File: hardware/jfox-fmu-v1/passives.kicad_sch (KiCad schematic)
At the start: 43 parts, among them X1 16MHz, X2 32.768kHz

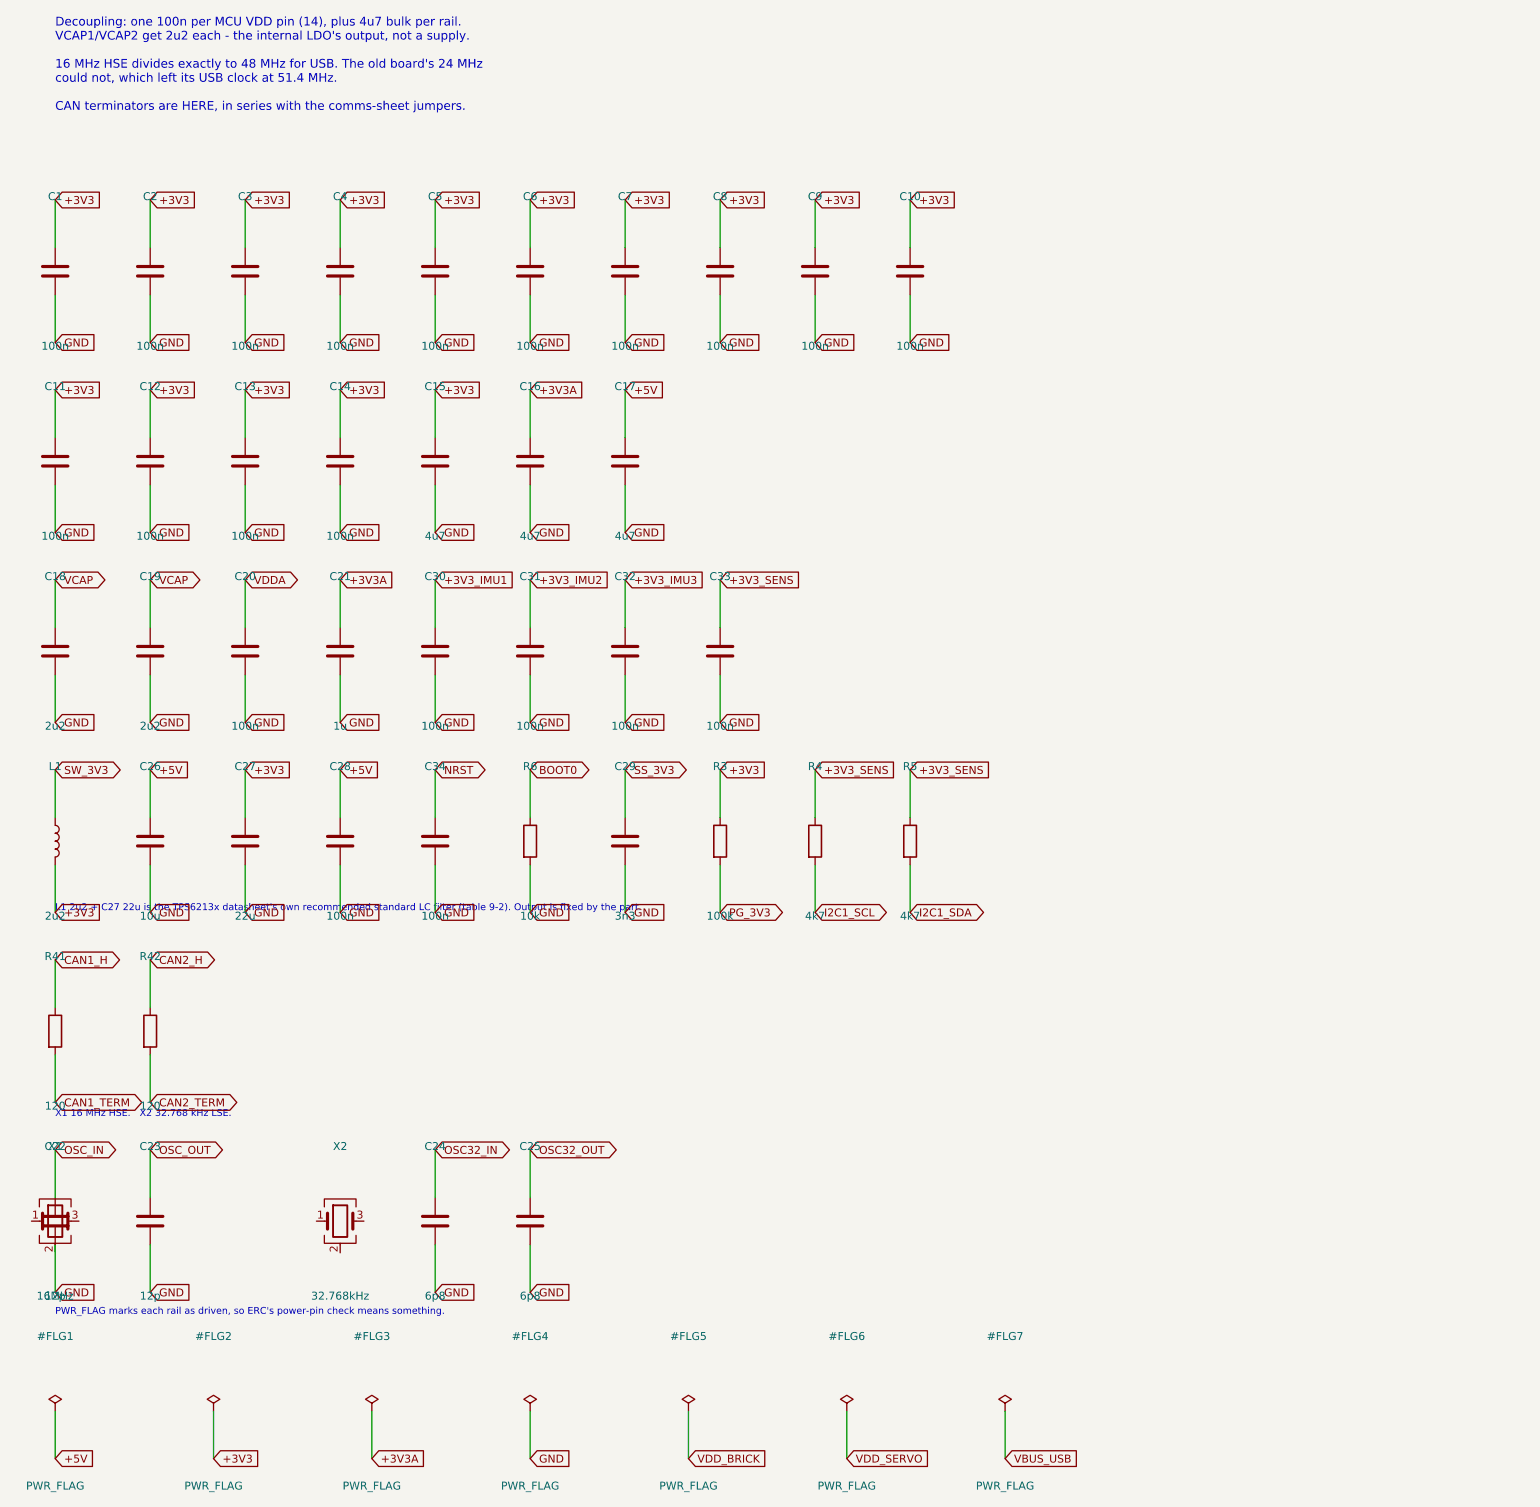
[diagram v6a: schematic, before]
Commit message: Isolated CAN FD, and the short it took a bisect to find
CAN redundancy is resolved by using Cyphal. FDCAN1 and FDCAN2 become two
redundant Cyphal/CAN interfaces on two independent isolated buses.

That is not the compromise it looked like. Cyphal handles redundancy in the
protocol: the specification defines redundant transport groups where a node
publishes on every interface and the receiver deduplicates, per frame or per
transfer. libcanard gives each redundant interface its own TX queue for
exactly this. So two controllers is the arrangement Cyphal is built around,
and it buys controller-level redundancy rather than the isolator-level
redundancy that keeping two separate buses would have given. The "four
controllers needed, two available" constraint dissolves rather than binds.

Better still, if wanted later: Cyphal supports heterogeneous redundancy, so a
Cyphal/CAN interface paired with Cyphal/UDP would give dissimilar transport
redundancy - the same argument that puts three IMUs from two vendors here.

U30/U31 become ISOW1044: isolated CAN FD with an integrated isolated DC-DC, so
each bus gets its own supply domain without a separate converter. Two
datasheet shorts that are easy to miss and both mandatory (SLLSFF7A table
7-1): GNDIO and GND1 are not internally connected, and VISOOUT/VSIN/VISOIN are
one node. EN/FLT is wired as the fault output with a 10k pull-up, because a
redundant link whose failure is silent is not redundant.

And the bug. Swapping an 8-pin TCAN332 for a 20-pin ISOW1044 while leaving the
row pitch at 44.45 mm overlapped the two transceivers - the ISOW1044 spans
35.56 mm and 50.8 mm with its stubs. Their stub ends coincided and merged the
rails. The netlist came out with no GND net and no +5V net at all: 171 pins on
+3V3, ground shorted to the supply across the entire board.

Nothing caught it. ERC does not object to a short - it is well-formed. The
page-fit and footprint checks passed. Even "all MCU supply pins sit on their
rail" passed, beca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
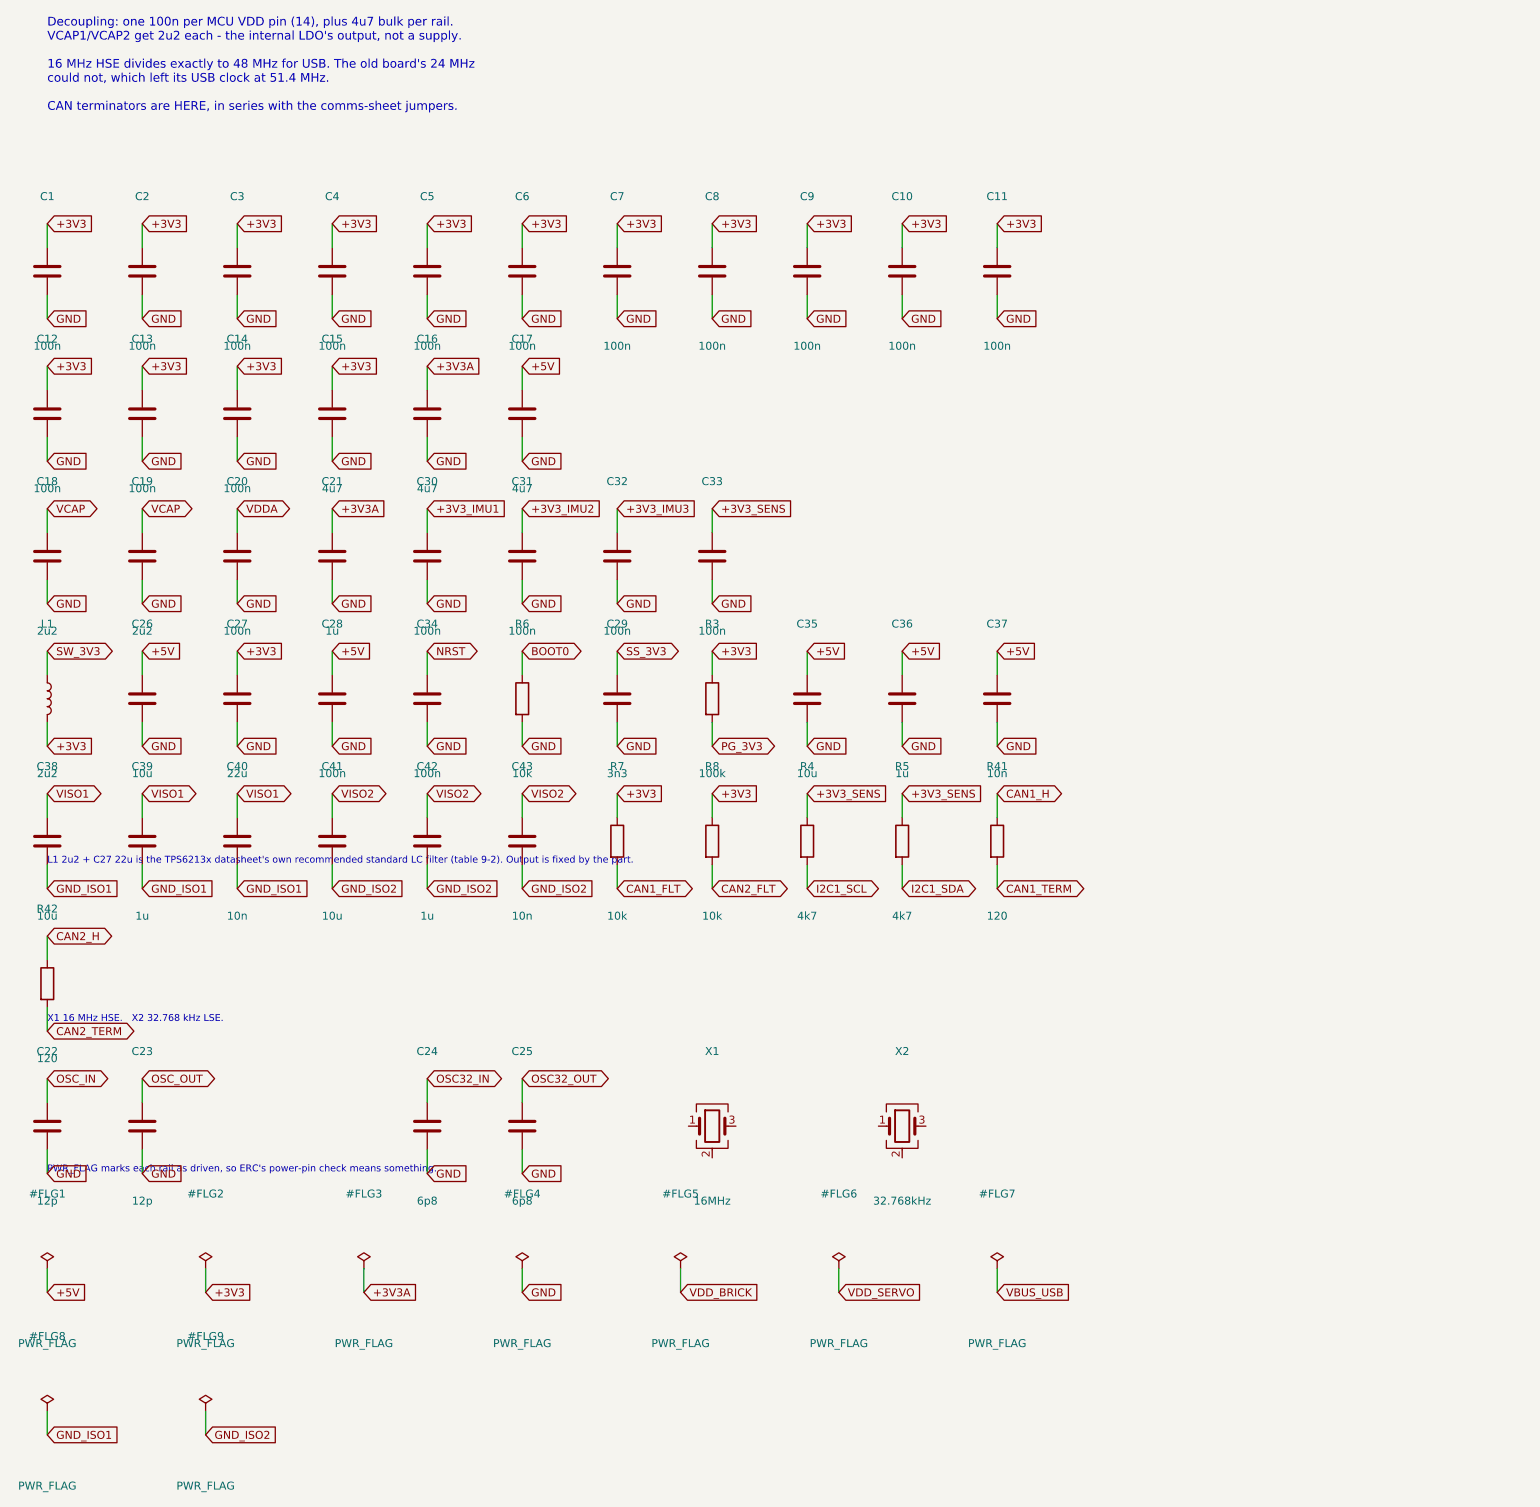
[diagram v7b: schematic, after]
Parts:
- added C35, C38, C41: 10u, Capacitor_SMD:C_0805_2012Metric, symbol Device:C
- added C36, C39, C42: 1u, Capacitor_SMD:C_0402_1005Metric, symbol Device:C
- added C37, C40, C43: 10n, Capacitor_SMD:C_0402_1005Metric, symbol Device:C
- added R7, R8: 10k, Resistor_SMD:R_0402_1005Metric, symbol Device:R
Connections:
- net +3V3: now also R7.1, R8.1
- net +5V: now also C35.1, C36.1, C37.1
- net GND: now also C35.2, C36.2, C37.2
- new net CAN1_FLT: R7.2
- new net CAN2_FLT: R8.2
- new net GND_ISO1: C38.2, C39.2, C40.2
- new net GND_ISO2: C41.2, C42.2, C43.2
- new net VISO1: C38.1, C39.1, C40.1
- new net VISO2: C41.1, C42.1, C43.1

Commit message: Five connections that went nowhere, and the pin name that hid one
None of these were visible as failures. Every one was a wire drawn to a name
that did not exist, which KiCad accepts silently.

wire_part matches by pin NAME. Four keys in the comms sheet matched nothing:

  "DAT3/CS"  the microSD symbol's pin is "CD/DAT3", so SDMMC1_D3 reached the
             MCU and stopped. The card would have run in 1-bit mode at best.
  "DET"      this symbol has no card-detect pin at all, so SD_DETECT had no
             source. Recorded rather than faked - it needs a socket symbol
             that exposes CD.
  "VSS2"     does not exist on this symbol.
  "SBU1/2"   do not exist on the USB-C symbol.

PC2 is the one worth remembering. On this package PC2 and PC3 exist only as
PC2_C and PC3_C - the analog-switch-capable balls. plan_pinout works from the
chip's alternate-function table, which calls them PC2 and PC3, so the lookup
missed and the allocated signal went nowhere. Aliased in both the generator
and the checker, which is what surfaced it: the check reported "symbol has no
pin named PC2" the moment the allocation grew enough to reach that pin.

Four parts that were missing outright, each leaving a function non-functional:

  R9/R10   5.1k on USB CC1/CC2. Without them the port is not a USB-C sink and
           no host will enumerate it. The CC pins reached the connector and
           nothing else.
  R11/R12  VBUS sense divider. VBUS_SENSE reached an ADC pin with nothing
           driving it. 10k/10k puts 5.25 V at 2.63 V, inside the reference.
  R13-R16  pull-ups on the four load-switch fault outputs, which are open
           drain and were unreadable without them.

And ten status signals now reach the MCU that previously reached nothing:
BRICK_VALID, SERVO_VALID, USB_VALID, PG_3V3, the four rail fault flags and
both isolator fault outputs. The board could not previously tell whether its
power source was valid, whether a sensor rail had tripped, or whether an
isolated 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
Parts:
- added R10, R9: 5k1, Resistor_SMD:R_0402_1005Metric, symbol Device:R
- added R11, R12, R13, R14, R15, R16: 10k, Resistor_SMD:R_0402_1005Metric, symbol Device:R
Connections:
- net +3V3: now also R13.1, R14.1, R15.1, R16.1
- net GND: now also R10.2, R12.2, R9.2
- net VBUS_USB: now also R11.1
- new net IMU1_RAIL_FLG: R13.2
- new net IMU2_RAIL_FLG: R14.2
- new net IMU3_RAIL_FLG: R15.2
- new net SENS_RAIL_FLG: R16.2
- new net USB_CC1: R9.1
- new net USB_CC2: R10.1
- new net VBUS_SENSE: R11.2, R12.1
